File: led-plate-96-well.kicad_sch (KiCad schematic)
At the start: 10 parts, among them J2 RAPC722X, U1 R-78E5.0-0.5, U2 A000053

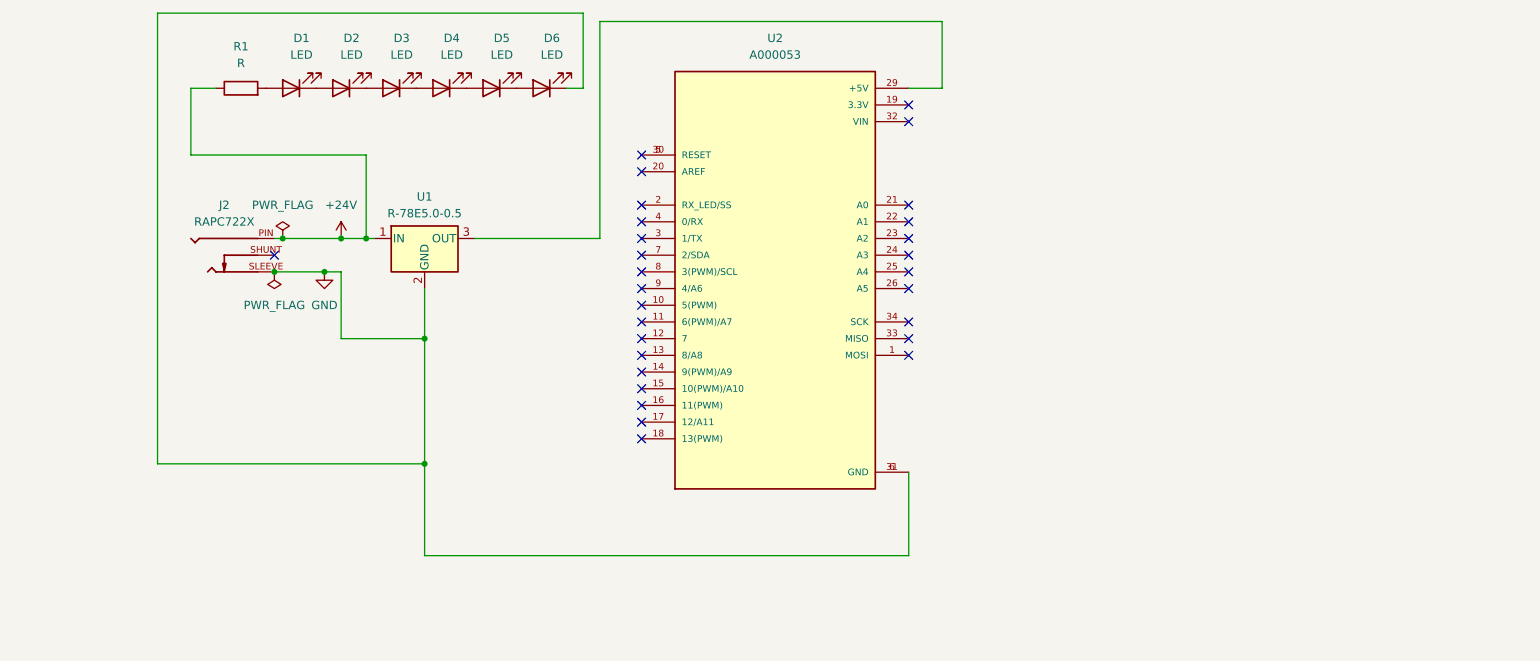
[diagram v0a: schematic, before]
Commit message: basic led layout started
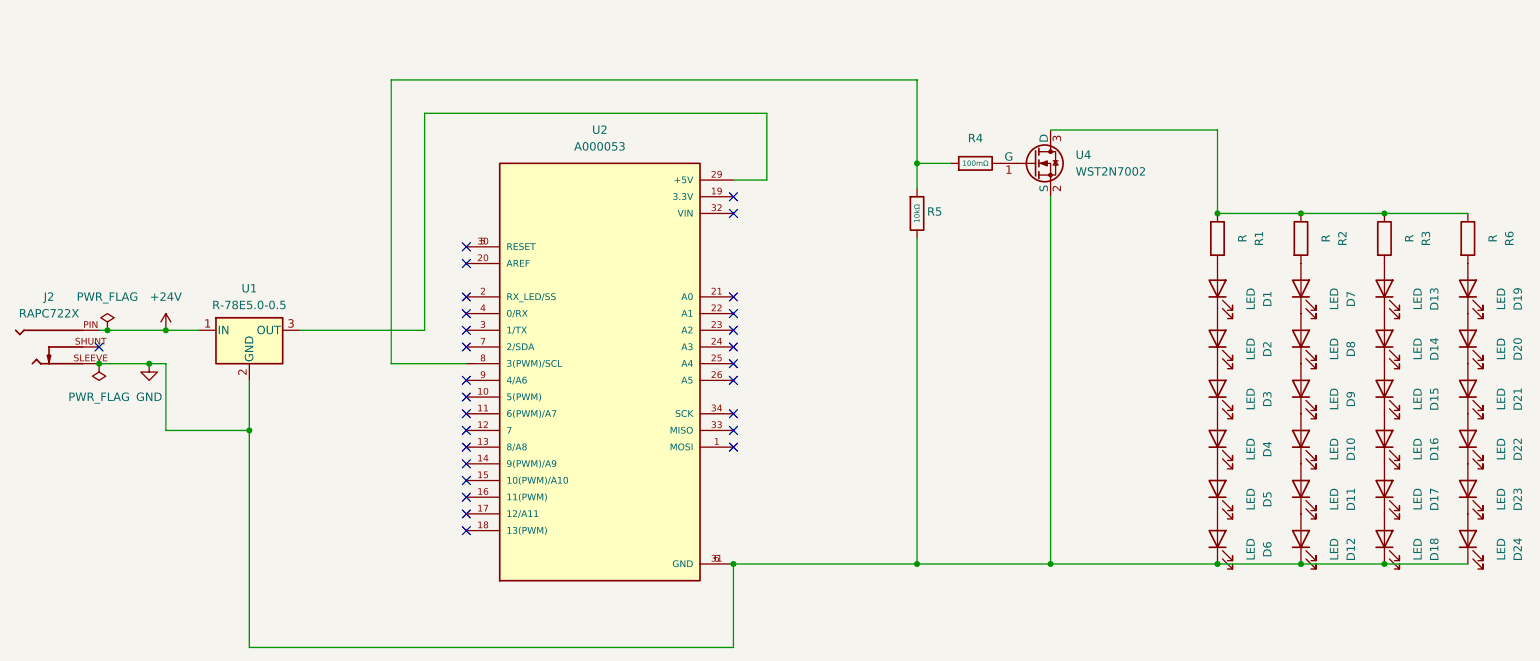
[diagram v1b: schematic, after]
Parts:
- added D10, D11, D12, D13, D14, D15, D16, D17, D18, D19, D20, D21, D22, D23, D24, D7, D8, D9: LED, LED_SMD:LED_Luminus_MP-3030-1100_3.0x3.0mm, symbol Device:LED
- added R2, R3, R6: R, Resistor_SMD:R_1210_3225Metric, symbol Device:R
- added R4: 100mΩ, PCM_JLCPCB:R_1206, symbol PCM_JLCPCB-Resistors:1206,100mΩ
- added R5: 10kΩ, PCM_JLCPCB:R_1206, symbol PCM_JLCPCB-Resistors:1206,10kΩ
- added U4: WST2N7002, Package_TO_SOT_SMD:SOT-23, symbol WST2N7002:WST2N7002
- U2: footprint arduino_micro:A000053 -> A000053:ARDUINO_A000053
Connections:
- net +24V: no longer R1.1
- net GND: now also D12.1 (K), D18.1 (K), D24.1 (K), R5.2, U4.2 (S)
- net at U2.8 (3(PWM)/SCL): now also R4.1, R5.1
- new net: D20.1 (K), D21.2 (A)
- new net: D19.1 (K), D20.2 (A)
- new net: D23.1 (K), D24.2 (A)
- new net: D13.1 (K), D14.2 (A)
- new net: D13.2 (A), R3.2
- new net: D10.2 (A), D9.1 (K)
- new net: D8.1 (K), D9.2 (A)
- new net: D19.2 (A), R6.2
- new net: D11.1 (K), D12.2 (A)
- new net: D10.1 (K), D11.2 (A)
- new net: D7.1 (K), D8.2 (A)
- new net: D7.2 (A), R2.2
- new net: R1.1, R2.1, R3.1, R6.1, U4.3 (D)
- new net: D17.1 (K), D18.2 (A)
- new net: D22.1 (K), D23.2 (A)
- new net: D21.1 (K), D22.2 (A)
- new net: R4.2, U4.1 (G)
- new net: D16.1 (K), D17.2 (A)
- new net: D15.1 (K), D16.2 (A)
- new net: D14.1 (K), D15.2 (A)
- no-connect marks 29 -> 28
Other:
- moved on the sheet: D1, D2, D3, D4, D5, D6, J2, R1, U1, U2

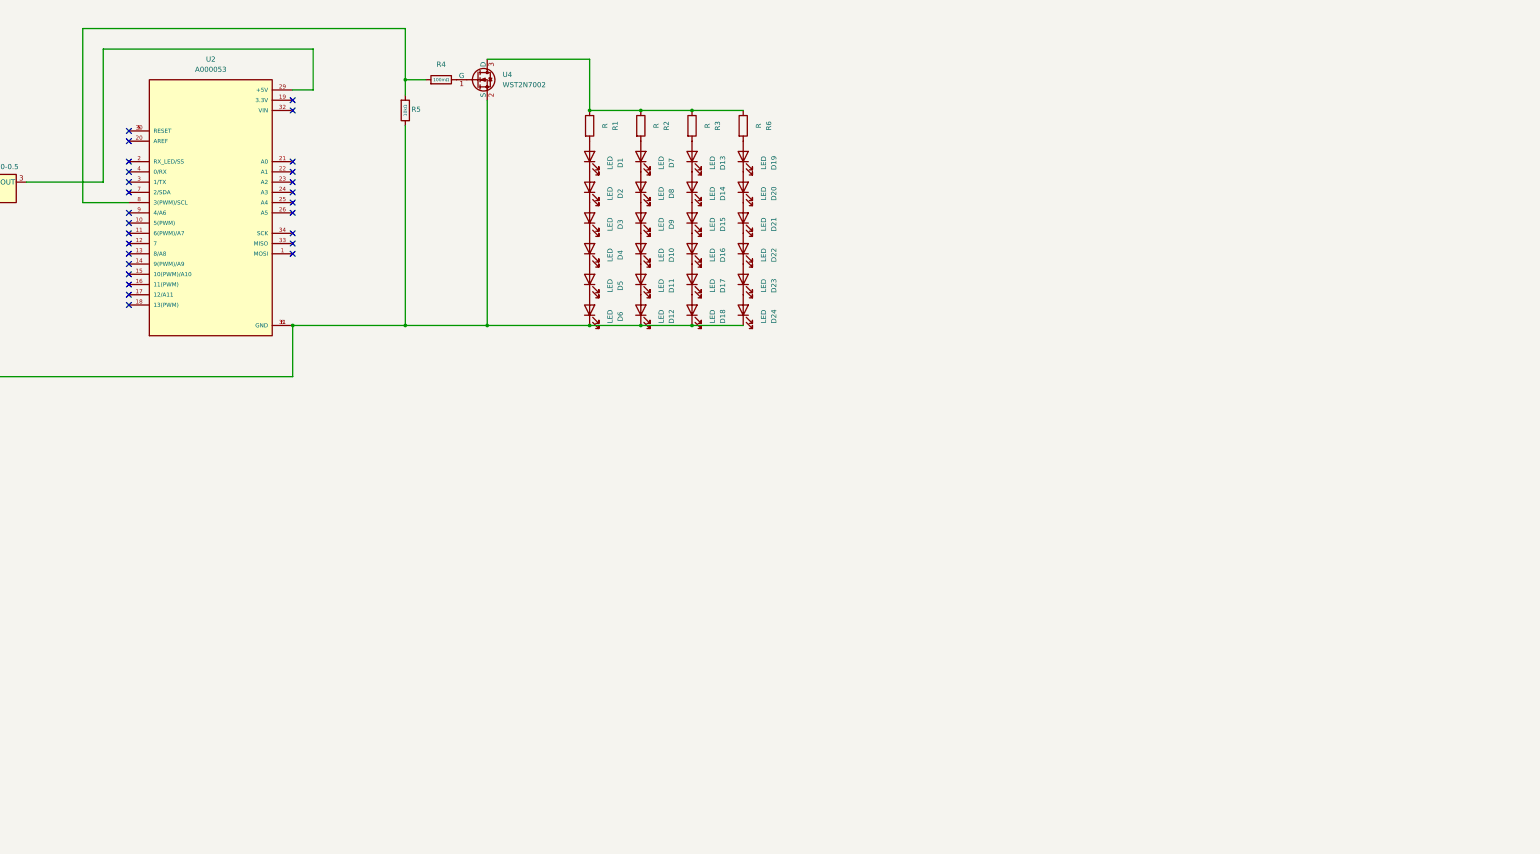
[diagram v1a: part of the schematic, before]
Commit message: all 96 leds laid out
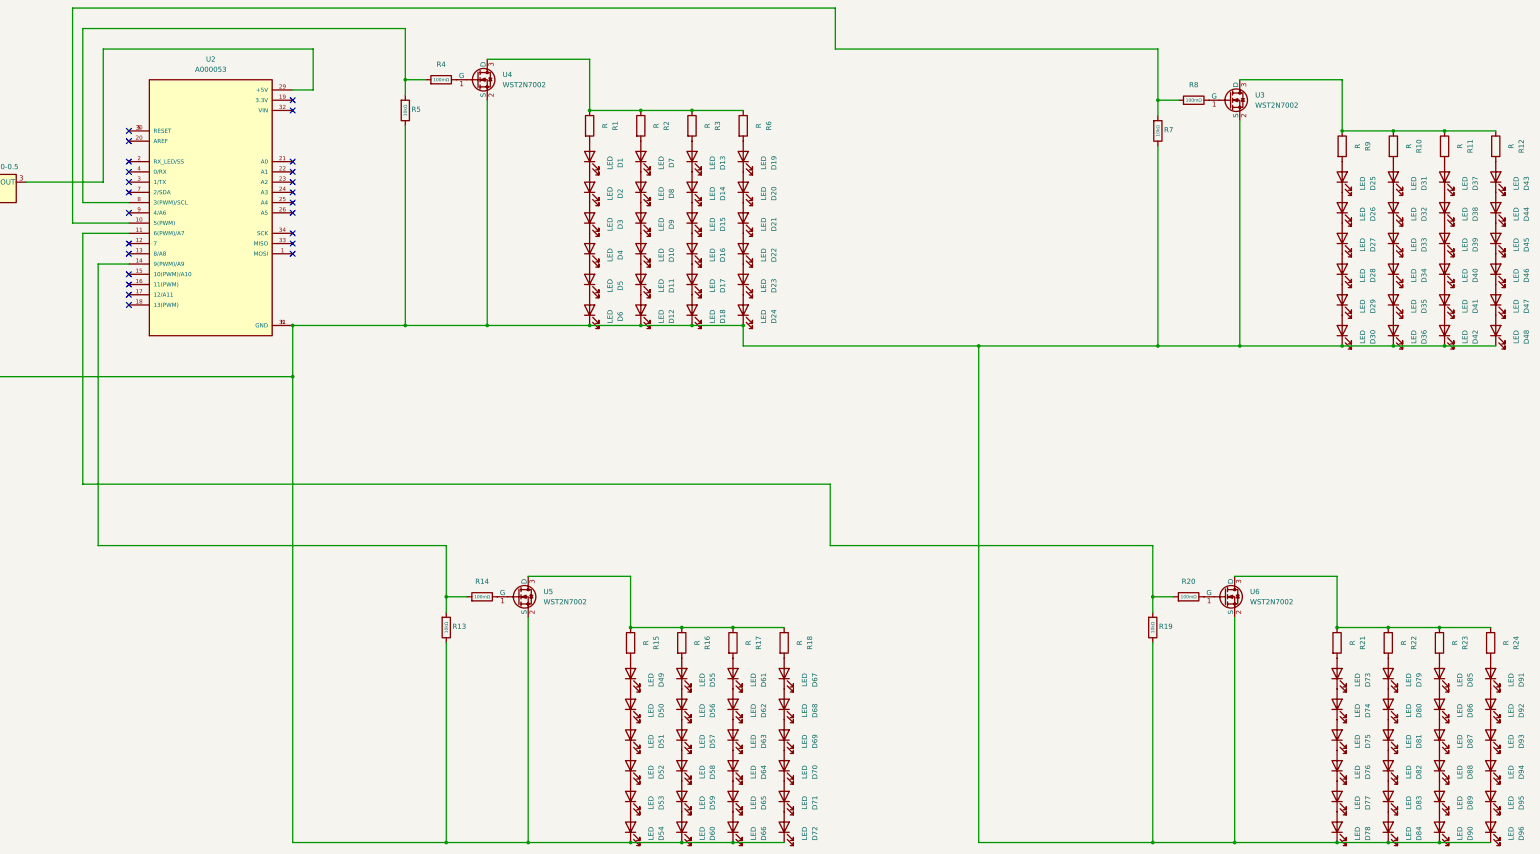
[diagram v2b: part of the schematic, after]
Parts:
- added D25, D26, D27, D28, D29, D30, D31, D32, D33, D34, D35, D36, D37, D38, D39, D40, D41, D42, D43, D44, D45, D46, D47, D48, D49, D50, D51, D52, D53, D54, D55, D56, D57, D58, D59, D60, D61, D62, D63, D64, D65, D66, D67, D68, D69, D70, D71, D72, D73, D74, D75, D76, D77, D78, D79, D80, D81, D82, D83, D84, D85, D86, D87, D88, D89, D90, D91, D92, D93, D94, D95, D96: LED, LED_SMD:LED_Luminus_MP-3030-1100_3.0x3.0mm, symbol Device:LED
- added R10, R11, R12, R15, R16, R17, R18, R21, R22, R23, R24, R9: R, Resistor_SMD:R_1210_3225Metric, symbol Device:R
- added R13, R19, R7: 10kΩ, PCM_JLCPCB:R_1206, symbol PCM_JLCPCB-Resistors:1206,10kΩ
- added R14, R20, R8: 100mΩ, PCM_JLCPCB:R_1206, symbol PCM_JLCPCB-Resistors:1206,100mΩ
- added U3, U5, U6: WST2N7002, Package_TO_SOT_SMD:SOT-23, symbol WST2N7002:WST2N7002
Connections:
- net GND: now also D30.1 (K), D36.1 (K), D42.1 (K), D48.1 (K), D54.1 (K), D60.1 (K), D66.1 (K), D72.1 (K), D78.1 (K), D84.1 (K), D90.1 (K), D96.1 (K), R13.2, R19.2, R7.2, U3.2 (S), U5.2 (S), U6.2 (S)
- net at U2.10 (5(PWM)): now also R7.1, R8.1
- net at U2.11 (6(PWM)/A7): now also R19.1, R20.1
- net at U2.14 (9(PWM)/A9): now also R13.1, R14.1
- new net: R21.1, R22.1, R23.1, R24.1, U6.3 (D)
- new net: D79.2 (A), R22.2
- new net: D39.1 (K), D40.2 (A)
- new net: D38.1 (K), D39.2 (A)
- new net: D51.1 (K), D52.2 (A)
- new net: D50.1 (K), D51.2 (A)
- new net: D32.1 (K), D33.2 (A)
- new net: D31.1 (K), D32.2 (A)
- new net: R10.1, R11.1, R12.1, R9.1, U3.3 (D)
- new net: D37.2 (A), R11.2
- new net: D57.1 (K), D58.2 (A)
- new net: D56.1 (K), D57.2 (A)
- new net: D43.1 (K), D44.2 (A)
- new net: D43.2 (A), R12.2
- new net: D27.1 (K), D28.2 (A)
- new net: D26.1 (K), D27.2 (A)
- new net: D79.1 (K), D80.2 (A)
- new net: D31.2 (A), R10.2
- new net: R20.2, U6.1 (G)
- new net: D41.1 (K), D42.2 (A)
- new net: D40.1 (K), D41.2 (A)
- new net: D25.1 (K), D26.2 (A)
- new net: D68.1 (K), D69.2 (A)
- new net: D67.1 (K), D68.2 (A)
- new net: D83.1 (K), D84.2 (A)
- new net: D91.2 (A), R24.2
- new net: D94.1 (K), D95.2 (A)
- new net: D93.1 (K), D94.2 (A)
- new net: D47.1 (K), D48.2 (A)
- new net: D46.1 (K), D47.2 (A)
- new net: D73.2 (A), R21.2
- new net: D89.1 (K), D90.2 (A)
- new net: D88.1 (K), D89.2 (A)
- new net: D65.1 (K), D66.2 (A)
- new net: D64.1 (K), D65.2 (A)
- new net: D52.1 (K), D53.2 (A)
- new net: D63.1 (K), D64.2 (A)
- new net: D62.1 (K), D63.2 (A)
- new net: D75.1 (K), D76.2 (A)
- new net: D74.1 (K), D75.2 (A)
- new net: D35.1 (K), D36.2 (A)
- new net: D92.1 (K), D93.2 (A)
- new net: D28.1 (K), D29.2 (A)
- new net: D55.1 (K), D56.2 (A)
- new net: R14.2, U5.1 (G)
- new net: R15.1, R16.1, R17.1, R18.1, U5.3 (D)
- new net: D37.1 (K), D38.2 (A)
- new net: D45.1 (K), D46.2 (A)
- new net: D95.1 (K), D96.2 (A)
- new net: D61.2 (A), R17.2
- new net: D55.2 (A), R16.2
- new net: D53.1 (K), D54.2 (A)
- new net: D67.2 (A), R18.2
- new net: D77.1 (K), D78.2 (A)
- new net: D82.1 (K), D83.2 (A)
- new net: D44.1 (K), D45.2 (A)
- new net: D87.1 (K), D88.2 (A)
- new net: D86.1 (K), D87.2 (A)
- new net: D85.1 (K), D86.2 (A)
- new net: D85.2 (A), R23.2
- new net: D81.1 (K), D82.2 (A)
- new net: D80.1 (K), D81.2 (A)
- new net: R8.2, U3.1 (G)
- new net: D91.1 (K), D92.2 (A)
- new net: D69.1 (K), D70.2 (A)
- new net: D71.1 (K), D72.2 (A)
- new net: D59.1 (K), D60.2 (A)
- new net: D58.1 (K), D59.2 (A)
- new net: D70.1 (K), D71.2 (A)
- new net: D61.1 (K), D62.2 (A)
- new net: D49.2 (A), R15.2
- new net: D29.1 (K), D30.2 (A)
- new net: D34.1 (K), D35.2 (A)
- new net: D76.1 (K), D77.2 (A)
- new net: D49.1 (K), D50.2 (A)
- new net: D33.1 (K), D34.2 (A)
- new net: D73.1 (K), D74.2 (A)
- new net: D25.2 (A), R9.2
- no-connect marks 28 -> 25

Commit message: set components and build again
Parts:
- R14, R20, R4, R8: value 100mΩ -> 100Ω
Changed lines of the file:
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@@
 			)
 		)
-		(property "Value" "100mΩ"
+		(property "Value" "100Ω"
 			(at 191.77 58.42 90)
 			(do_not_autoplace yes)
@@
 			)
 		)
-		(property "Datasheet" "https://www.lcsc.com/datasheet/lcsc_datasheet_2205311900_UNI-ROYAL-Uniroyal-Elec-1206W4F100LT5E_C25334.pdf"
+		(property "Datasheet" ""
 			(at 191.77 58.42 0)
 			(effects
@@
 			)
 		)
-		(property "Value" "100mΩ"
+		(property "Value" "100Ω"
 			(at 378.46 63.5 90)
 			(do_not_autoplace yes)
@@
 			)
 		)
-		(property "Datasheet" "https://www.lcsc.com/datasheet/lcsc_datasheet_2205311900_UNI-ROYAL-Uniroyal-Elec-1206W4F100LT5E_C25334.pdf"
+		(property "Datasheet" ""
 			(at 378.46 63.5 0)
 			(effects
@@
 			)
 		)
-		(property "Value" "100mΩ"
+		(property "Value" "100Ω"
 			(at 201.93 186.69 90)
 			(do_not_autoplace yes)
@@
 			)
 		)
-		(property "Datasheet" "https://www.lcsc.com/datasheet/lcsc_datasheet_2205311900_UNI-ROYAL-Uniroyal-Elec-1206W4F100LT5E_C25334.pdf"
+		(property "Datasheet" ""
 			(at 201.93 186.69 0)
 			(effects
@@
 			)
 		)
-		(property "Value" "100mΩ"
+		(property "Value" "100Ω"
 			(at 377.19 186.69 90)
 			(do_not_autoplace yes)
@@
 			)
 		)
-		(property "Datasheet" "https://www.lcsc.com/datasheet/lcsc_datasheet_2205311900_UNI-ROYAL-Uniroyal-Elec-1206W4F100LT5E_C25334.pdf"
+		(property "Datasheet" ""
 			(at 377.19 186.69 0)
 			(effects
